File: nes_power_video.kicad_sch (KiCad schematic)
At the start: 22 parts, among them J2 Audio, J3 Video, J4 Conn_01x05, J5 RGB conn feed, Q1 2SA1015, U1 TPS2553DBV

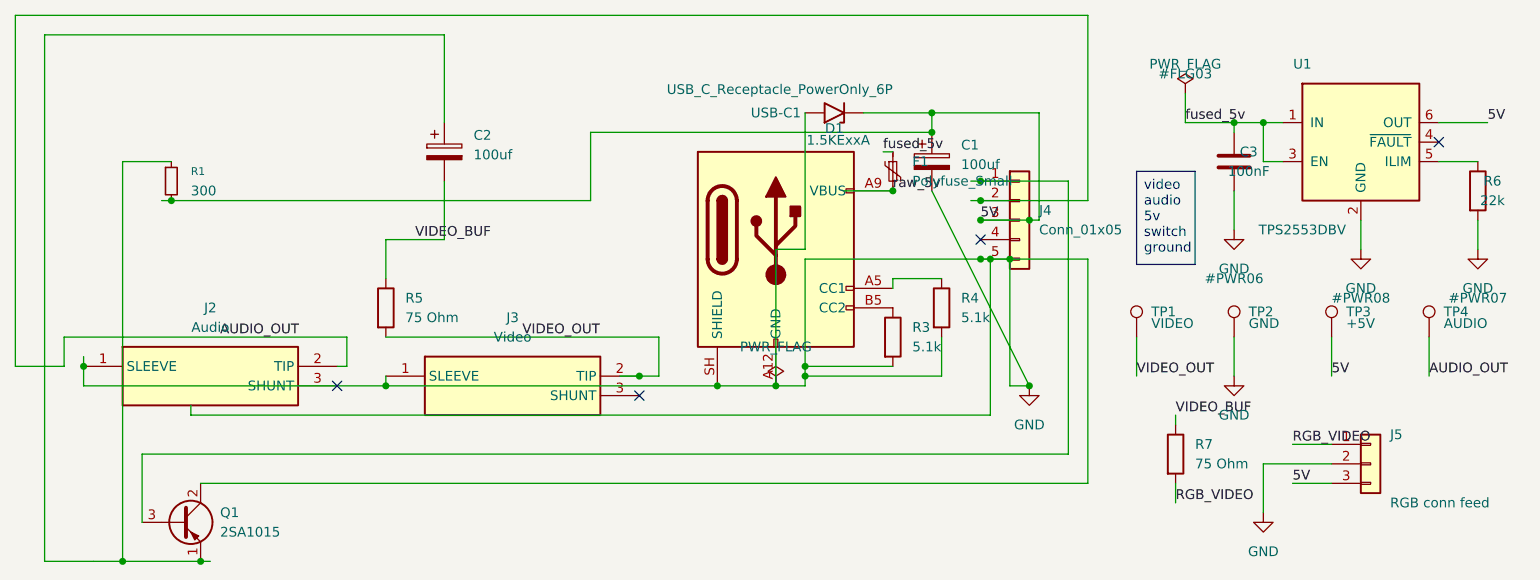
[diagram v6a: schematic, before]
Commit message: Clear all ERC warnings: prune dead wires, fix footprint links
Removes 10 wires left stranded by earlier edits, including two dead
branches (the y=175.26 GND run and its drop to y=154.94) that only
became visible once the 1.27 mm stubs in front of them were gone.

Every removal was gated on the exported netlist staying byte-identical,
one wire at a time. That check earned its keep: it refused
(27.94,194.31)->(38.1,194.31), which looks like a stub but carries Q1's
connection. An earlier attempt that judged wires by computing pin
positions instead got the rotation math wrong and cut live nets on U1
and R4 -- reverted, and not how this was done.

Also drops an orphaned junction dot at (128.27,146.05), and prefixes the
J2/J3 Footprint fields with the nes1: library nickname. Without the
prefix KiCad resolves the library name as "", so the next
schematic-to-PCB sync could not have matched those footprints.

Removes the stale "Saturn 8pin mini DIN mod" sym-lib-table entry, which
pointed at a file that does not exist and threw an error on project open.
That connector was ruled out in favour of the NESRGB mini-DIN.

ERC is now 0 errors / 0 warnings, from 10. DRC unchanged at 2 pre-existing
silkscreen warnings / 0 unconnected. Netlist identical to before the
cleanup, and all 17 nets still cross-check between schematic and PCB.

Co-Authored-By: Claude Opus 5 <noreply@anthropic.com>
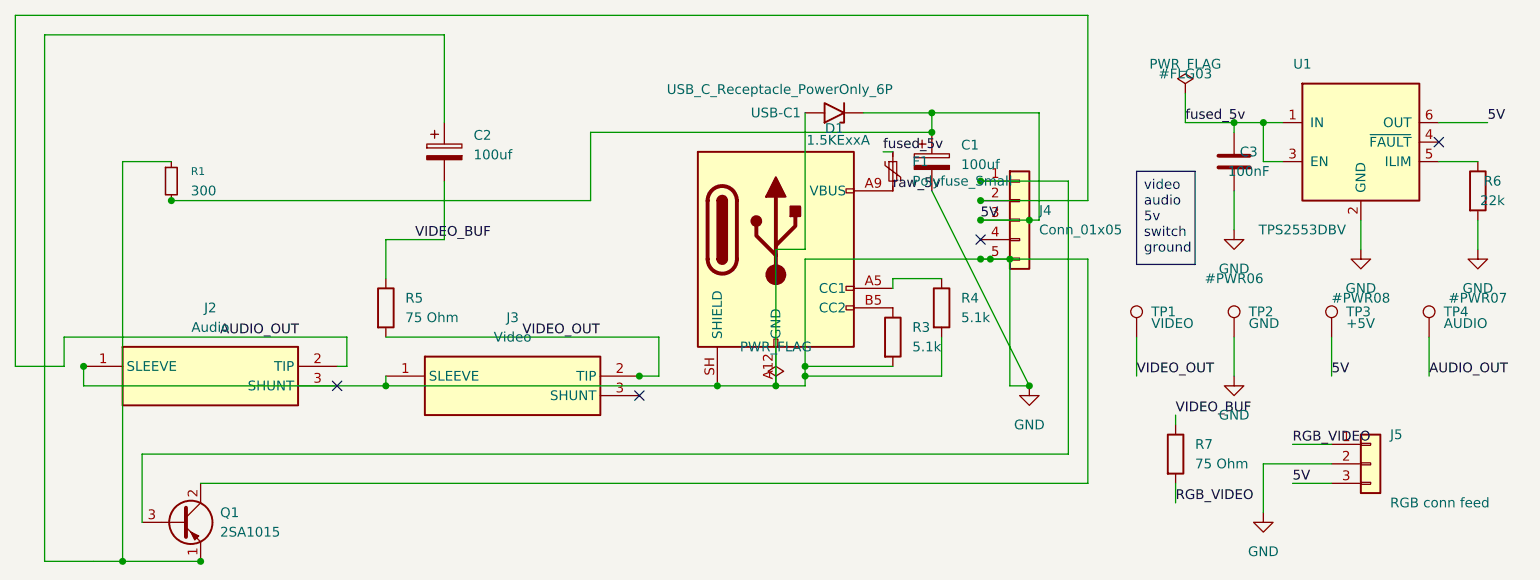
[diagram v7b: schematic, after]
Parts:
- J2, J3: footprint PJRAN1X1U03X -> nes1:PJRAN1X1U03X
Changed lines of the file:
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@@
-	)
-	(junction
-		(at 128.27 146.05)
-		(diameter 0)
-		(color 0 0 0 0)
 	)
 	(junction
@@
 	(wire
 		(pts
-			(xy 36.83 175.26) (xy 140.97 175.26)
-		)
-		(stroke
-			(width 0)
-			(type default)
-		)
-	)
-	(wire
-		(pts
 			(xy 24.13 194.31) (xy 27.94 194.31)
 		)
@@
 	(wire
 		(pts
-			(xy 22.86 167.64) (xy 22.86 168.91)
-		)
-		(stroke
-			(width 0)
-			(type default)
-		)
-	)
-	(wire
-		(pts
 			(xy 143.51 154.94) (xy 143.51 171.45)
 		)
@@
 	(wire
 		(pts
-			(xy 140.97 175.26) (xy 140.97 154.94)
-		)
-		(stroke
-			(width 0)
-			(type default)
-		)
-	)
-	(wire
-		(pts
-			(xy 121.92 146.05) (xy 128.27 146.05)
-		)
-		(stroke
-			(width 0)
-			(type default)
-		)
-	)
-	(wire
-		(pts
-			(xy 33.02 147.32) (xy 34.29 147.32)
-		)
-		(stroke
-			(width 0)
-			(type default)
-		)
-	)
-	(wire
-		(pts
-			(xy 36.83 173.99) (xy 36.83 175.26)
-		)
-		(stroke
-			(width 0)
-			(type default)
-		)
-	)
-	(wire
-		(pts
 			(xy 13.97 168.91) (xy 13.97 123.19)
 		)
@@
 	(wire
 		(pts
-			(xy 138.43 144.78) (xy 139.7 144.78)
-		)
-		(stroke
-			(width 0)
-			(type default)
-		)
-	)
-	(wire
-		(pts
 			(xy 95.25 170.18) (xy 97.79 170.18)
 		)
@@
 	(wire
 		(pts
-			(xy 38.1 194.31) (xy 39.37 194.31)
-		)
-		(stroke
-			(width 0)
-			(type default)
-		)
-	)
-	(wire
-		(pts
 			(xy 133.35 146.05) (xy 146.05 171.45)
 		)
@@
 		(pts
 			(xy 116.84 170.18) (xy 116.84 168.91)
-		)
-		(stroke
-			(width 0)
-			(type default)
-		)
-	)
-	(wire
-		(pts
-			(xy 138.43 147.32) (xy 139.7 147.32)
-		)
-		(stroke
-			(width 0)
-			(type default)
-		)
-	)
-	(wire
-		(pts
-			(xy 92.71 170.18) (xy 95.25 170.18)
 		)
 		(stroke
@@
 			)
 		)
-		(property "Footprint" "PJRAN1X1U03X"
+		(property "Footprint" "nes1:PJRAN1X1U03X"
 			(at 91.44 265.1 0)
 			(hide yes)
@@
 			)
 		)
-		(property "Footprint" "PJRAN1X1U03X"
+		(property "Footprint" "nes1:PJRAN1X1U03X"
 			(at 52.07 263.83 0)
 			(hide yes)

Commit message: v2 design fixes: R1 to 220R, add R2 base resistor, silkscreen values
R1 300R -> 220R. At the assumed ~1.3V base, 300-330R supplies only ~6.2mA at
peak white against the ~6.7mA the 150R load (R5 75R + TV 75R) needs, so the
follower clips on bright content. 220R gives ~9.3mA.

Add R2, 330R in series between J4 pin 1 and Q1's base, mirroring the 330R
Nintendo places in the same position. Negligible against Q1's ~21k base input
impedance; limits fault current into the base-emitter junction, whose reverse
rating is only 5V. Netlist verified: Net-(Q1-E) is unchanged and 16 of 17
existing nets are byte-identical.

Print all resistor and capacitor values on the silkscreen. R1/R3/R4/R5/R7
share one axial footprint across four values with nothing to tell them apart,
which produced three separate wrong-resistor errors in R1 on the prototype.

C2 to 470uF in the BOM to match what the design needs: into the 150R load,
100uF gives tau=15ms against the 16.7ms field period. F1 value field carried
the library name instead of a rating.

README: document why the board exists (the RF modulator cooks its own
electrolytics - three for three on the bench), the video input biasing and the
1k pulldown the NES mainboard supplies, KSA1015 sourcing for the obsolete
2SA1015, and the lead-trimming requirement for bottom-side clearance.

ERC 0 violations. DRC 2 pre-existing J2/J3 silk warnings, 0 unconnected.

Co-Authored-By: Claude Opus 5 <noreply@anthropic.com>
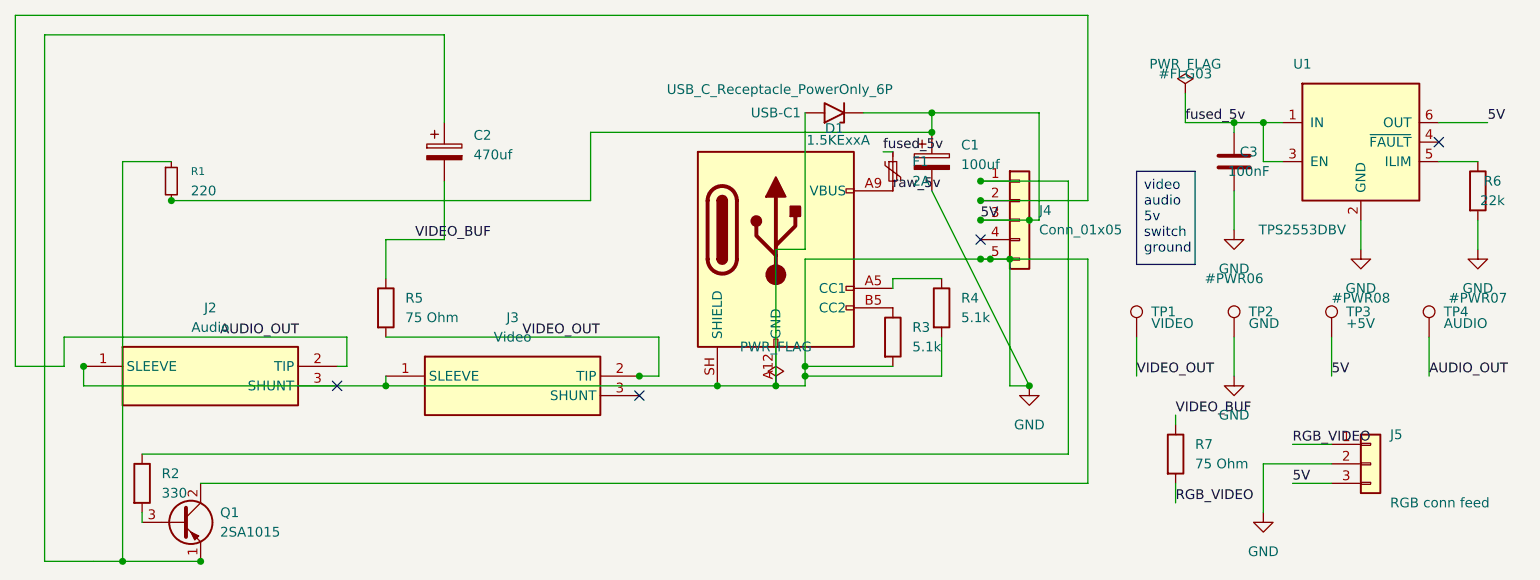
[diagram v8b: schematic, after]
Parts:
- added R2: 330, Resistor_THT:R_Axial_DIN0207_L6.3mm_D2.5mm_P7.62mm_Horizontal, symbol Device:R
- C2: value 100uf -> 470uf
- F1: value Polyfuse_Small -> 2A
- R1: value 300 -> 220
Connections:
- net at Q1.3 (B): now also R2.2; no longer J4.1 (Pin_1)
- new net: J4.1 (Pin_1), R2.1
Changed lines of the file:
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@@
 	(wire
 		(pts
-			(xy 30.48 189.23) (xy 30.48 180.34)
+			(xy 30.48 189.23) (xy 30.48 187.96)
 		)
 		(stroke
@@
 			)
 		)
-		(property "Value" "100uf"
+		(property "Value" "470uf"
 			(at 73.66 141.3509 0)
 			(show_name no)
@@
 			)
 		)
-		(property "Value" "Polyfuse_Small"
+		(property "Value" "2A"
 			(at 130.81 144.7799 0)
 			(show_name no)
@@
 				(path "/467ff530-bd7b-4486-a282-e5127feecbd3"
 					(reference "F1")
+					(unit 1)
+				)
+			)
+		)
+	)
+	(symbol
+		(lib_id "Device:R")
+		(at 30.48 184.15 0)
+		(unit 1)
+		(body_style 1)
+		(exclude_from_sim no)
+		(in_bom yes)
+		(on_board yes)
+		(in_pos_files yes)
+		(dnp no)
+		(fields_autoplaced yes)
+		(property "Reference" "R2"
+			(at 33.02 182.8799 0)
+			(show_name no)
+			(do_not_autoplace no)
+			(effects
+				(font
+					(size 1.27 1.27)
+				)
+				(justify left)
+			)
+		)
+		(property "Value" "330"
+			(at 33.02 185.4199 0)
+			(show_name no)
+			(do_not_autoplace no)
+			(effects
+				(font
+					(size 1.27 1.27)
+				)
+				(justify left)
+			)
+		)
+		(property "Footprint" "Resistor_THT:R_Axial_DIN0207_L6.3mm_D2.5mm_P7.62mm_Horizontal"
+			(at 28.702 184.15 90)
+			(hide yes)
+			(show_name no)
+			(do_not_autoplace no)
+			(effects
+				(font
+					(size 1.27 1.27)
+				)
+			)
+		)
+		(property "Datasheet" ""
+			(at 30.48 184.15 0)
+			(hide yes)
+			(show_name no)
+			(do_not_autoplace no)
+			(effects
+				(font
+					(size 1.27 1.27)
+				)
+			)
+		)
+		(property "Description" "Resistor"
+			(at 30.48 184.15 0)
+			(hide yes)
+			(show_name no)
+			(do_not_autoplace no)
+			(effects
+				(font
+					(size 1.27 1.27)
+				)
+			)
+		)
+		(pin "1"
+		)
+		(pin "2"
+		)
+		(instances
+			(project "nes_power_video"
+				(path "/467ff530-bd7b-4486-a282-e5127feecbd3"
+					(reference "R2")
 					(unit 1)
 				)
@@
 			)
 		)
-		(property "Value" "300"
+		(property "Value" "220"
 			(at 36.83 146.0499 0)
 			(show_name no)
